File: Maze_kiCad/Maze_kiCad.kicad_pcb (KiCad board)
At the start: 2 copper layers, 32 parts, among them J1 Screw_Terminal, J10 pins: 42_41_40_39_38_37, J11 pins: 42_41_40_39_38_37, J12 Vcc/Gnd, J2 motor2, J3 motor1, J4 Vmm/Mode, J5 INT/ADO/XCL/XDA, J6 GND, J7 IR Receiver, J8 pins: 5v/12_11_10_9_46, J9 pins: 3.3v/RST/43_44_2, U1 ESP32-S3-DevKitC-1, U10 Reg S7V7F5, U2 TCRT5000, U3 TCRT5000, U4 TCRT5000, U5 TCRT5000, U6 TCRT5000, U7 TCRT5000, U8 Gyro mpu-6050, U9 HC-SR04

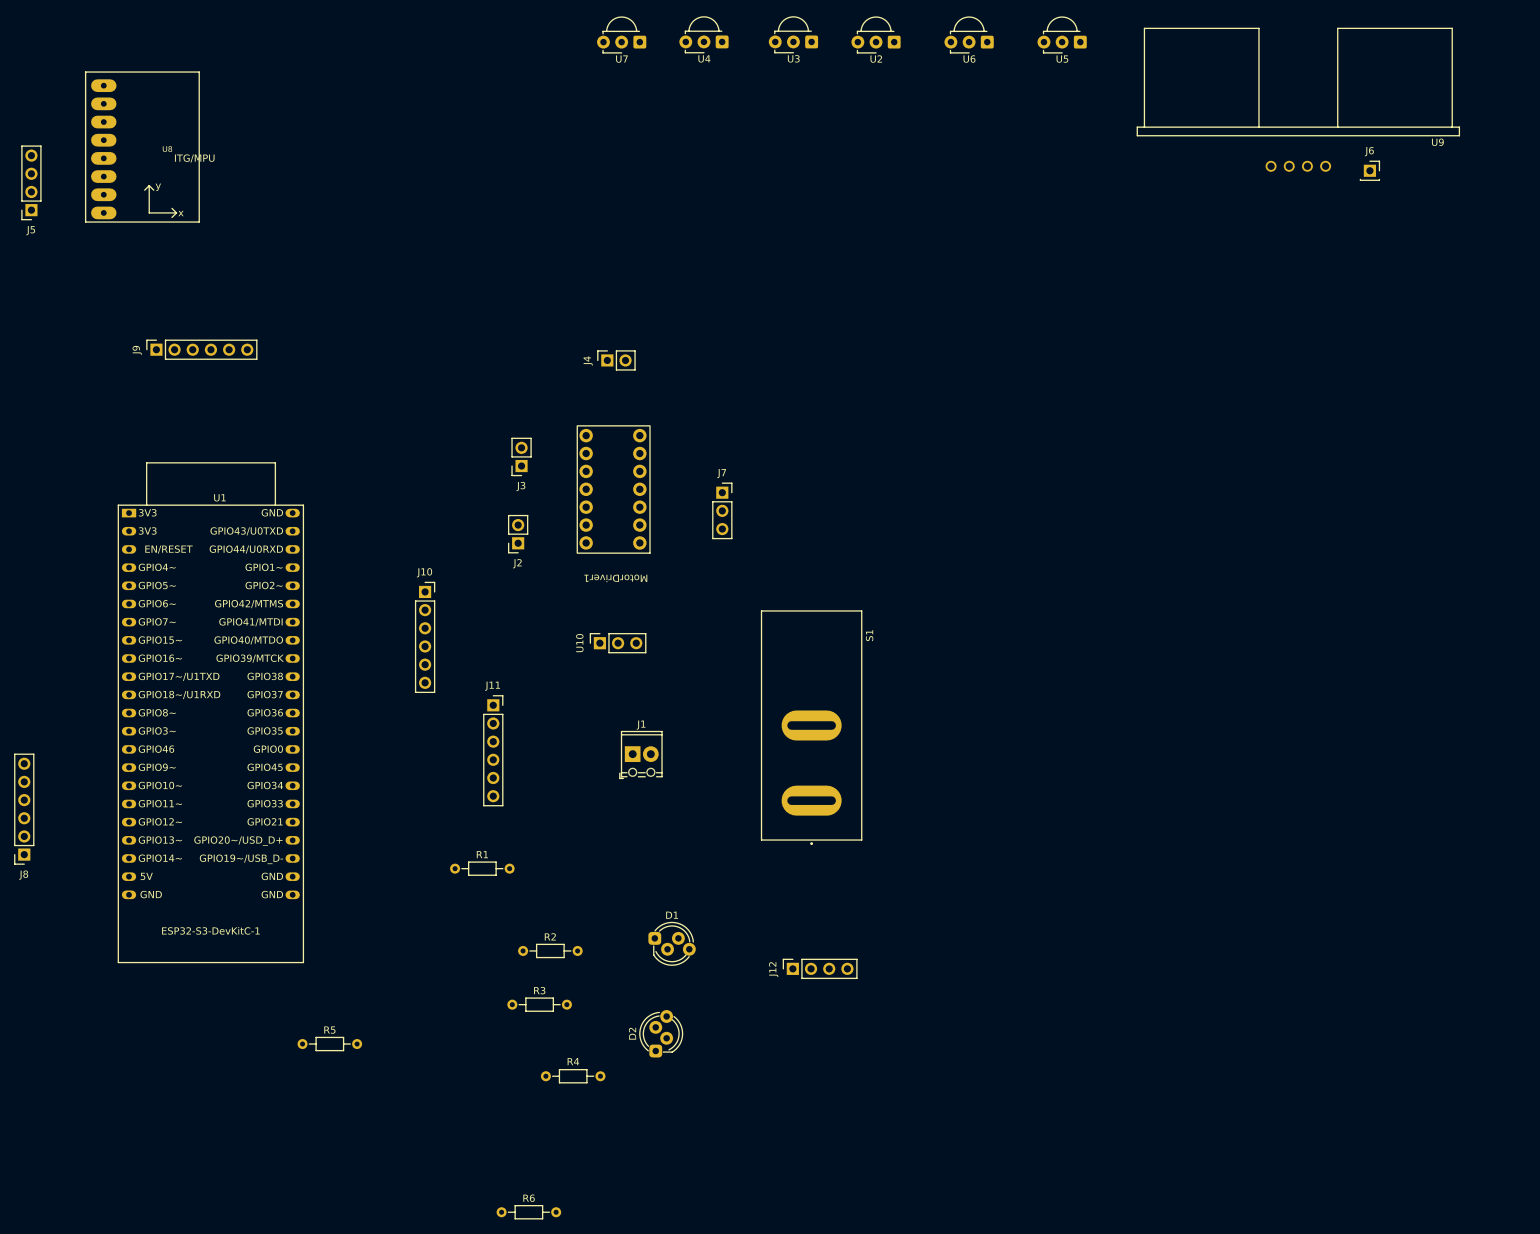
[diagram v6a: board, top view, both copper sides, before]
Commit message: Create version 1 of pcb
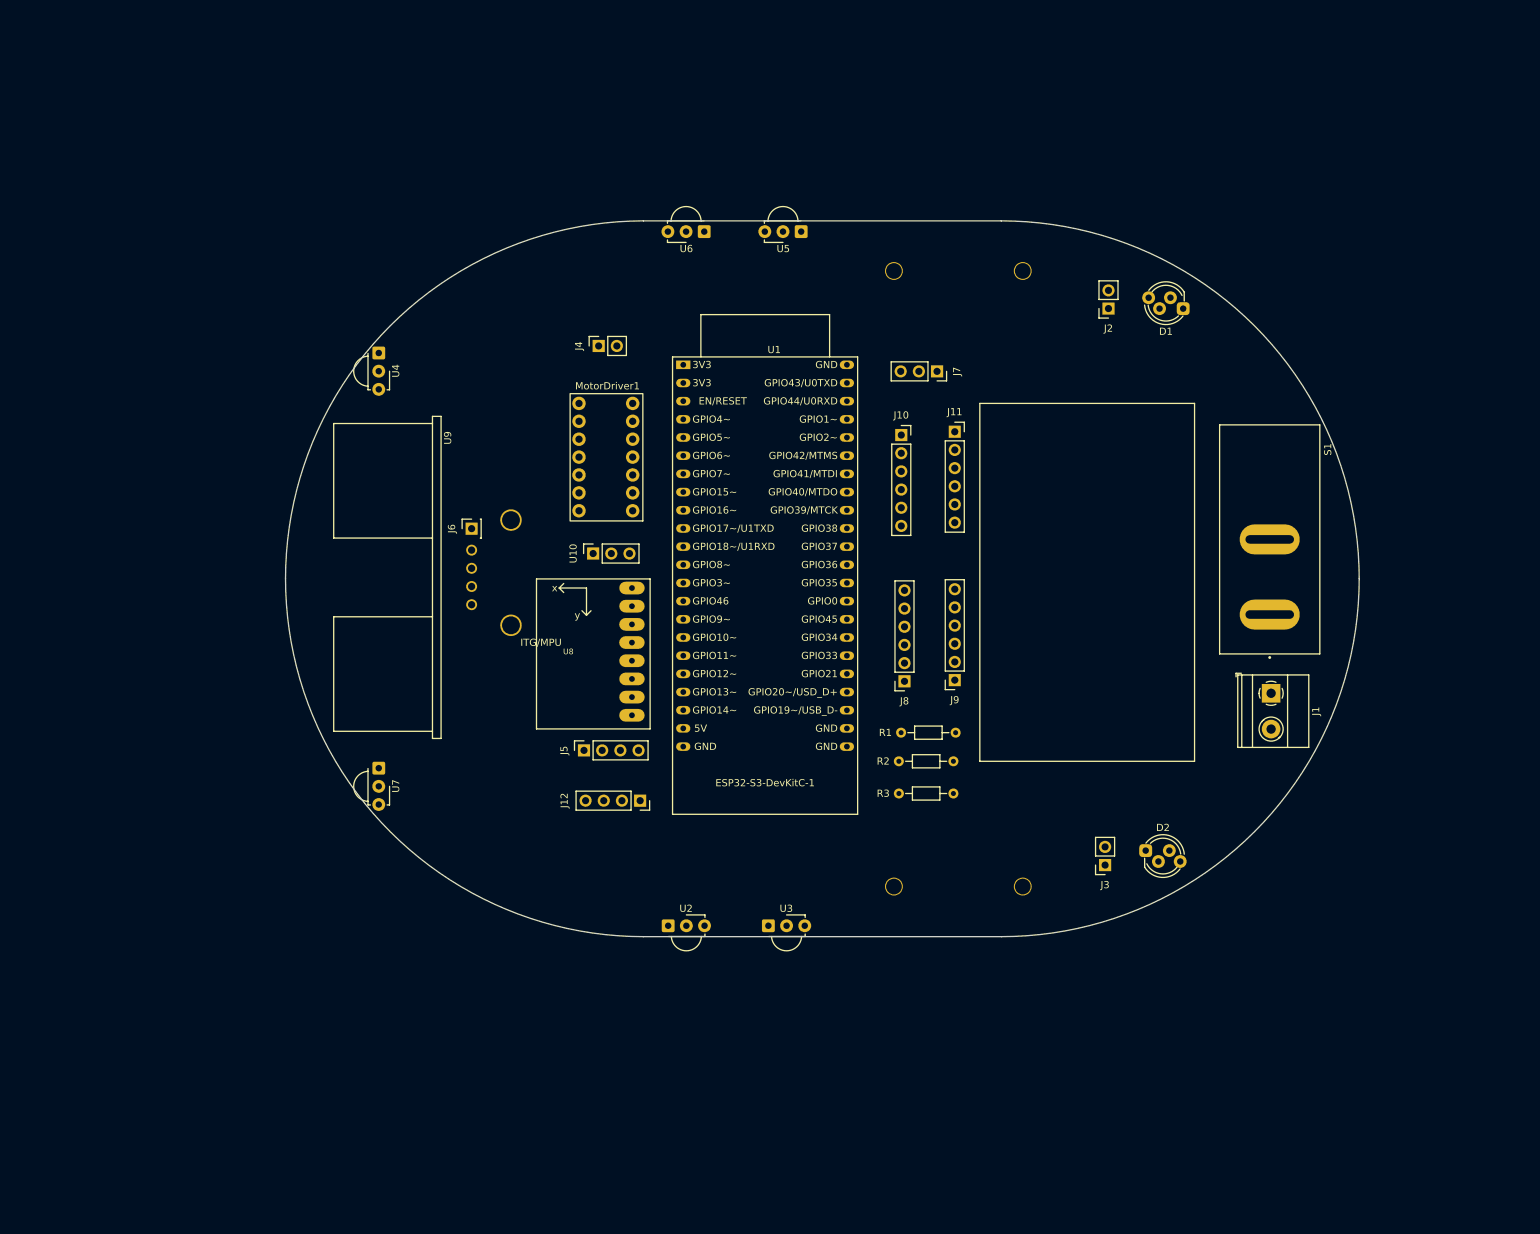
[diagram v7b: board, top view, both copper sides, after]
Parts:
- removed R4, R5, R6: 220-ohm, Resistor_THT:R_Axial_DIN0204_L3.6mm_D1.6mm_P7.62mm_Horizontal
- added ?: , , F.Cu at (145.5, 141.5)
- added ?: , , F.Cu at (163.5, 141.5)
- added ?: , , F.Cu at (163.5, 55.5)
- added ?: , , F.Cu at (92.0, 90.3)
- added ?: , , F.Cu at (92.0, 105.0)
- added ?: , , F.Cu at (145.5, 55.5)
- J1: footprint TerminalBlock_Phoenix:TerminalBlock_Phoenix_MPT-0,5-2-2.54_1x02_P2.54mm_Horizontal -> TerminalBlock_Phoenix:TerminalBlock_Phoenix_MKDS-1,5-2_1x02_P5.00mm_Horizontal
- moved J6 135.1 mm to (86.5, 91.5), turned to 90 degrees
- moved U9 129.0 mm to (86.5, 98.3), turned to -90 degrees
- moved U2 127.4 mm to (114.0, 147.0), turned to 0 degrees
- moved J8 125.3 mm to (147.0, 112.8)
- moved U3 123.6 mm to (128.0, 147.0), turned to 0 degrees
- moved J9 120.7 mm to (154.0, 112.7), turned to 180 degrees
- moved D1 114.8 mm to (185.9, 60.8), turned to 180 degrees
- moved J5 108.0 mm to (102.2, 122.5), turned to 90 degrees
- moved U7 107.8 mm to (73.5, 125.0), turned to -90 degrees
- moved J3 98.8 mm to (175.0, 138.5)
- moved U8 89.8 mm to (100.0, 108.7), turned to 180 degrees
- moved J1 89.6 mm to (198.2, 114.5), turned to -90 degrees
- moved J2 88.8 mm to (175.5, 60.8)
- moved U1 80.2 mm to (116.1, 68.6)
- moved J11 74.9 mm to (154.0, 78.0)
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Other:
- board outline added: 150 x 100 mm

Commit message: Final maze robot pcb
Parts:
- added ?: , , F.Cu at (170.0, 135.0)
- added ?: , , F.Cu at (100.0, 135.0)
- added ?: , , F.Cu at (100.0, 60.0)
- added ?: , , F.Cu at (170.0, 60.0)
- J11: value pins: 42_41_40_39_38_37 -> gnd_gnd_45_0_35_36
- J7: moved to B.Cu
- moved J4 46.9 mm to (150.2, 75.0)
- moved J12 35.1 mm to (143.0, 117.5), turned to 0 degrees
- moved J3 28.0 mm to (149.2, 127.5), turned to 90 degrees
- moved J2 24.6 mm to (152.5, 69.6), turned to -90 degrees
- moved R3 12.4 mm to (148.0, 116.2), turned to -90 degrees
- moved R2 8.89 mm to (150.5, 116.2), turned to -90 degrees
- moved J7 7.54 mm to (144.0, 70.0), turned to 180 degrees
- moved R1 7.51 mm to (153.0, 116.2), turned to -90 degrees
- moved U10 4.16 mm to (102.0, 91.1)
- moved J8 3.72 mm to (143.5, 111.6)
- moved U1 3.50 mm to (112.6, 68.6)
- moved J10 3.38 mm to (143.5, 79.9)
- moved MotorDriver1 3.16 mm to (104.5, 78.6)
- moved J5 3.00 mm to (99.2, 122.5)
- moved J11 2.47 mm to (152.5, 79.9)
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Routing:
- net GND: track 0.00 -> 448.9 mm, vias 0 -> 4
- net VCC: track 0.00 -> 315.6 mm, vias 0 -> 2
- net Net-(J3-Pin_2): track 0.00 -> 142.2 mm, vias 0 -> 1
- net Net-(D1-RA): track 0.00 -> 141.6 mm, vias 0 -> 1
- net Net-(J3-Pin_1): track 0.00 -> 129.1 mm, vias 0 -> 1
- net GND2: track 0.00 -> 117.2 mm
- net +7V: track 0.00 -> 115.1 mm, vias 0 -> 2
- net Net-(D1-GA): track 0.00 -> 111.5 mm, vias 0 -> 2
- net Net-(D1-BA): track 0.00 -> 104.6 mm, vias 0 -> 2
- net Net-(J2-Pin_1): track 0.00 -> 70.6 mm
- net Net-(J2-Pin_2): track 0.00 -> 62.8 mm
- net /trig_pin20: track 0.00 -> 61.3 mm
- net /echo_pin19: track 0.00 -> 60.1 mm
- net Net-(J9-Pin_1): track 0.00 -> 58.3 mm
- net /ir_sensor_2: track 0.00 -> 57.9 mm, vias 0 -> 1
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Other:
- board text added: "0"
- board text added: "10"
- board text added: "11"
- board text added: "12"
- board text added: "2"
- board text added: "3.3V"
- board text added: "35"
- board text added: "36"
- board text added: "37"
- board text added: "38"
- board text added: "39"
- board text added: "40"
- board text added: "41"
- board text added: "42"
- board text added: "43"
- board text added: "44"
- board text added: "45"
- board text added: "46"
- board text added: "5V"
- board text added: "7V"
- board text added: "9"
- board text added: "Battery"
- board text added: "GND"
- board text added: "VCC"
- board text added: "ado"
- board text added: "gnd"
- board text added: "in"
- board text added: "int"
- board text added: "rst"
- board text added: "vcc"
- board text added: "vmm MD"
- board text added: "xcl"
- board text added: "xda"
